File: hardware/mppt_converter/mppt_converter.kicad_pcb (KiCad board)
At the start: 4 copper layers, 130 x 65 mm, 60 parts, among them J101 CT3151, J102 CT3151, J103 CT3151, J104 CT3151, Q101 EPC2059, Q102 EPC2059, Q103 BSS127S, U101 ADUM4221-1ARIZ

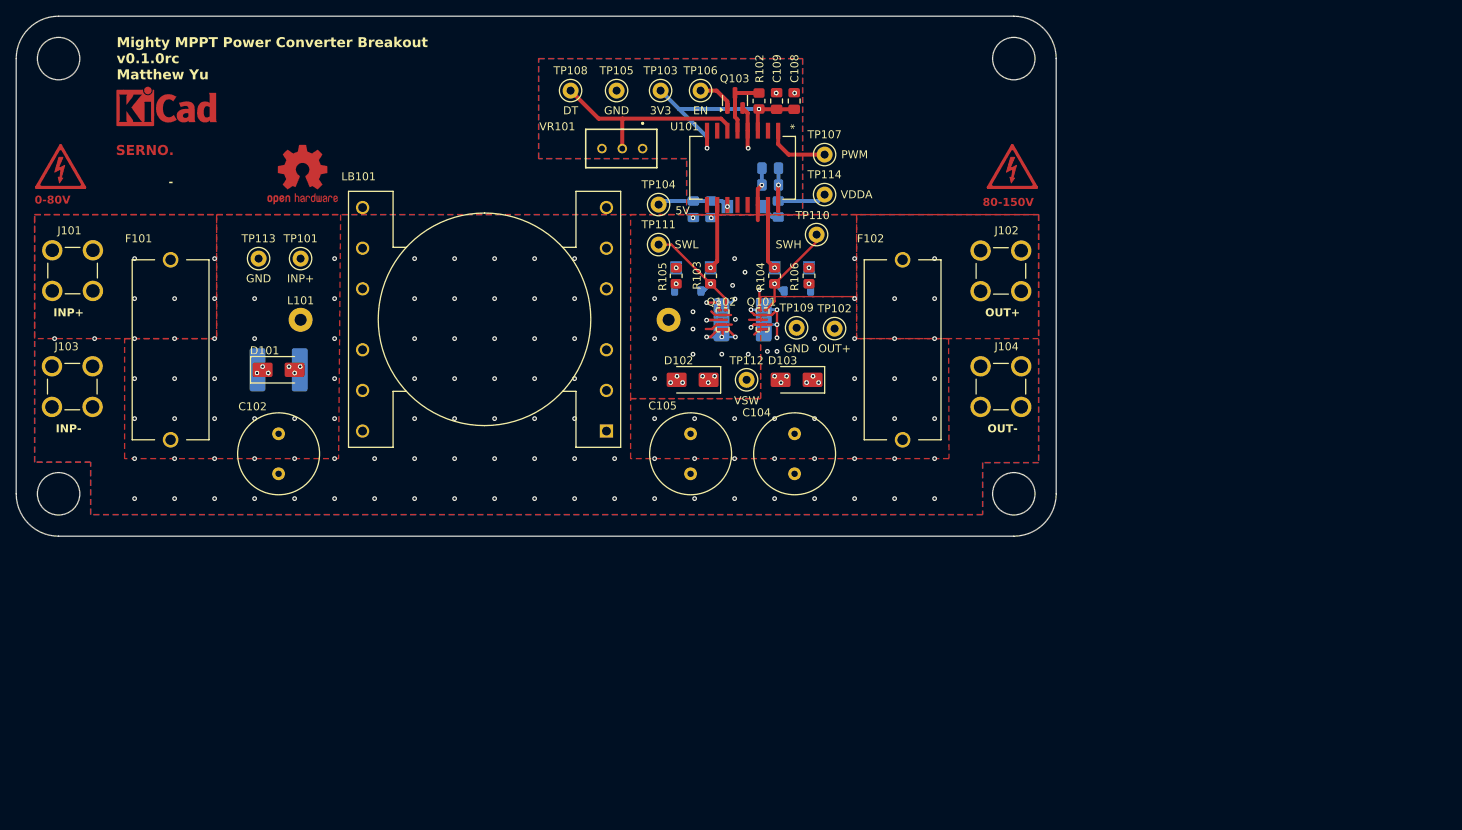
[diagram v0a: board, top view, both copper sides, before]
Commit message: changed layout of switching loop planes, added small 100n capacitors on HV input and output
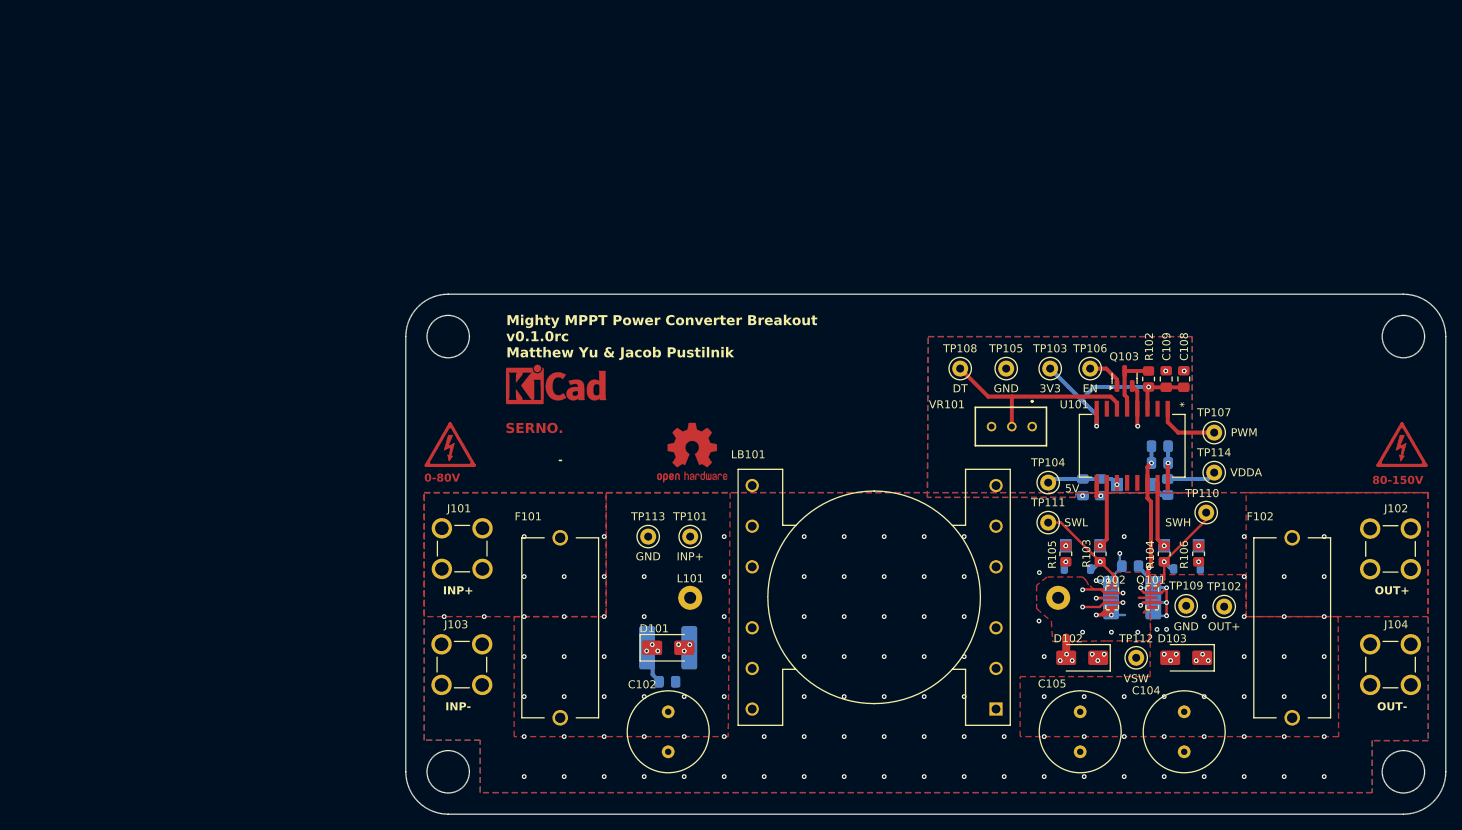
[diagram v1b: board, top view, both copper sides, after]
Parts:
- added C112: 100n, Capacitor_SMD:C_0805_2012Metric_Pad1.18x1.45mm_HandSolder, B.Cu at (106.1, 107.9)
- added C113: 100n, Capacitor_SMD:C_0805_2012Metric_Pad1.18x1.45mm_HandSolder, B.Cu at (163.9, 93.5)
- moved C110 59.8 mm to (158.1, 83.6)
- moved D107 59.8 mm to (158.1, 90.9)
- moved J102 59.8 mm to (196.5, 91.3)
- moved D106 59.8 mm to (171.1, 93.8)
- moved J104 59.8 mm to (196.5, 105.8)
- moved C101 59.8 mm to (106.2, 103.7)
- moved C102 59.8 mm to (106.2, 111.7)
- moved C106 59.8 mm to (167.7, 78.5)
- moved C107 59.8 mm to (167.7, 80.5)
- moved C108 59.8 mm to (170.7, 70.0)
- moved C111 59.8 mm to (160.2, 83.6)
- moved D101 59.8 mm to (106.2, 103.7)
- moved F101 59.8 mm to (92.7, 101.2)
- moved H101 59.8 mm to (78.7, 119.2)
- moved H102 59.8 mm to (78.7, 64.8)
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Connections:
- net Net-(D101-K) renamed /VIN_fused
- net Net-(D103-K) renamed /VOUT
- net Net-(D104-K) renamed /VBOOT_inner
- net Net-(Q103-D) renamed /DISABLE
- net Net-(U101-VDDA) renamed /VBOOT
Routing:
- net /VSW: track 19.0 -> 45.7 mm, vias 14 -> 13
- net /VOUT: track 18.2 -> 26.9 mm
- net GND: track 26.7 -> 32.7 mm, vias 138 -> 137
- net /VIN_fused: track 0.94 -> 5.85 mm
- net +3V3: track 28.7 -> 27.8 mm
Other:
- board text added: "Mighty MPPT Power Converter Breakout v0.1.0rc Matthew Yu & Jacob Pustilnik"
- board text removed: "Mighty MPPT Power Converter Breakout v0.1.0rc Matthew Yu"

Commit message: fix drc errors introduced into converter, power reg
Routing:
- net /VSW: track 45.7 -> 55.5 mm
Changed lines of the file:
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@@
 	(title_block
 		(title "Mighty MPPT Power Converter Breakout")
-		(date "2024-08-25")
+		(date "2024-08-27")
 		(rev "v0.1.0rc")
 		(comment 1 "Matthew Yu")
+		(comment 2 "Jacob Pustilnik")
 	)
 	(layers
@@
 				(font
 					(size 1 1)
-					(thickness 0.15)
+					(thickness 0.2)
 				)
 			)
@@
 				(font
 					(size 1 1)
-					(thickness 0.15)
+					(thickness 0.2)
 				)
 			)
@@
 				(font
 					(size 1 1)
-					(thickness 0.15)
+					(thickness 0.2)
 				)
 			)
@@
 				(font
 					(size 1 1)
-					(thickness 0.15)
+					(thickness 0.2)
 				)
 			)
@@
 				(font
 					(size 1 1)
-					(thickness 0.15)
+					(thickness 0.2)
 				)
 			)
@@
 				(font
 					(size 1 1)
-					(thickness 0.15)
+					(thickness 0.2)
 				)
 			)
@@
 				(font
 					(size 1 1)
-					(thickness 0.15)
+					(thickness 0.2)
 				)
 			)
@@
 				(font
 					(size 1 1)
-					(thickness 0.15)
+					(thickness 0.2)
 				)
 			)
@@
 				(font
 					(size 1 1)
-					(thickness 0.15)
+					(thickness 0.2)
 				)
 			)
@@
 				(font
 					(size 1 1)
-					(thickness 0.15)
+					(thickness 0.2)
 				)
 			)
@@
 				(font
 					(size 1 1)
-					(thickness 0.15)
+					(thickness 0.2)
 				)
 			)
@@
 				(font
 					(size 1 1)
-					(thickness 0.15)
+					(thickness 0.2)
 				)
 			)
@@
 				(font
 					(size 1 1)
-					(thickness 0.15)
+					(thickness 0.2)
 				)
 			)
@@
 				(font
 					(size 1 1)
-					(thickness 0.15)
+					(thickness 0.2)
 				)
 			)
@@
 				(font
 					(size 1 1)
-					(thickness 0.15)
+					(thickness 0.2)
 				)
 			)
@@
 				(font
 					(size 1 1)
-					(thickness 0.15)
+					(thickness 0.2)
 				)
 			)
@@
 				(font
 					(size 1 1)
-					(thickness 0.15)
+					(thickness 0.2)
 				)
 				(justify mirror)
@@
 				(font
 					(size 1 1)
-					(thickness 0.15)
+					(thickness 0.2)
 				)
 				(justify mirror)
@@
 			(effects
 				(font
-					(size 0.5 0.5)
-					(thickness 0.08)
+					(size 1 1)
+					(thickness 0.2)
 				)
 				(justify mirror)
@@
 		(tags "capacitor handsolder")
 		(property "Reference" "C112"
-			(at 0 1.68 0)
+			(at -3.9 -0.1 0)
 			(layer "B.SilkS")
 			(effects
 				(font
 					(size 1 1)
-					(thickness 0.15)
+					(thickness 0.2)
 				)
 				(justify mirror)
@@
 				(font
 					(size 1 1)
-					(thickness 0.15)
+					(thickness 0.2)
 				)
 				(justify mirror)
@@
 			(effects
 				(font
-					(size 0.5 0.5)
-					(thickness 0.08)
+					(size 1 1)
+					(thickness 0.2)
 				)
 				(justify mirror)
@@
 		(layer "Dwgs.User")
 		(pts
-			(xy 189.190255 126.850005) (xy 89.140255 126.950005)
-		)
-		(height -9.75)
-		(gr_text "100.0500 mm"
-			(at 139.173801 135.450001 0.05726712687)
-			(layer "Dwgs.User")
-			(effects
-				(font
-					(size 1 1)
-					(thickness 0.2)
-				)
-			)
-		)
-		(format
-			(prefix "")
-			(suffix "")
-			(units 3)
-			(units_format 1)
-			(precision 4)
-		)
-		(style
-			(thickness 0.05)
-			(arrow_length 1.27)
-			(text_position_mode 0)
-			(extension_height 0.58642)
-			(extension_offset 0.5) keep_text_aligned)
-	)
-	(dimension
-		(type aligned)
-		(layer "Dwgs.User")
-		(pts
 			(xy 178.45 114.899999) (xy 175.95 114.899999)
 		)
@@
 		(layer "Dwgs.User")
 		(pts
-			(xy 78.7 24.4) (xy 78.7 124.45)
+			(xy 78.7 59.2) (xy 78.7 124.45)
 		)
 		(height 7)
-		(gr_text "100.0500 mm"
-			(at 70.55 74.425 90)
+		(gr_text "65.2500 mm"
+			(at 70.55 91.825 90)
 			(layer "Dwgs.User")
 			(effects
@@
 	)
 	(segment
+		(start 164.7 101.9)
+		(end 164.9 101.7)
+		(width 0.75)
+		(layer "In1.Cu")
+		(net 10)
+	)
+	(segment
 		(start 156 103.25)
 		(end 155.85 103.25)
@@
 	)
 	(segment
+		(start 172.5 92.9)
+		(end 171.75 93.65)
+		(width 0.35)
+		(layer "In1.Cu")
+		(net 10)
+	)
+	(segment
+		(start 164.7 104.9)
+		(end 164.7 101.9)
+		(width 0.75)
+		(layer "In1.Cu")
+		(net 10)
+	)
+	(segment
 		(start 156 104.45)
 		(end 155.2 105.25)
@@
 	)
 	(segment
+		(start 171.75 93.65)
+		(end 166.3 93.65)
+		(width 0.35)
+		(layer "In1.Cu")
+		(net 10)
+	)
+	(segment
 		(start 156 104.45)
 		(end 156 104.55)
@@
 		(layers "F.Cu" "In1.Cu")
 		(hatch edge 0.5)
-		(priority 2)
+		(priority 1)
 		(connect_pads yes
 			(clearance 0.5)
@@
 		(polygon
 			(pts
-				(xy 138.7 64.75) (xy 171.7 64.75) (xy 171.7 84.2801) (xy 157.2 84.2801) (xy 157.1 84.85) (xy 138.6 84.85)
+				(xy 138.7 64.75) (xy 171.7 64.75) (xy 171.7 84.2801) (xy 157.1 84.35) (xy 138.7 84.3)
 			)
 		)
